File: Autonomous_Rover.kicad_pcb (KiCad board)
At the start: 2 copper layers, 112 x 65 mm, 40 parts, among them M2_1 MountingHole_Pad, M2_2 MountingHole_Pad, M2_3 MountingHole_Pad, Q1 AO3400A, Q2 AO3400A

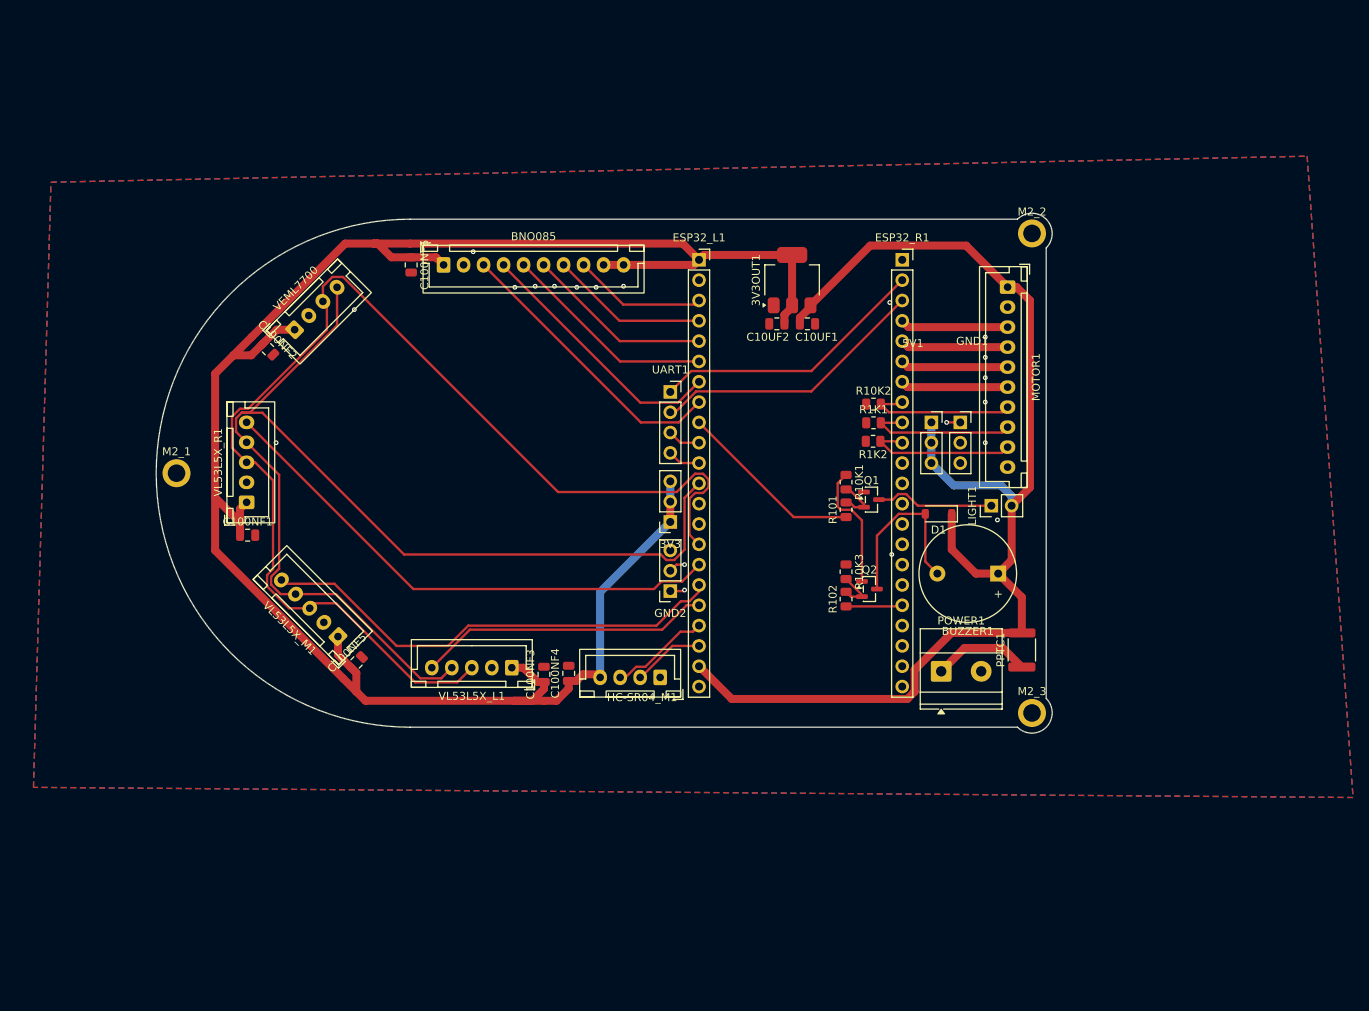
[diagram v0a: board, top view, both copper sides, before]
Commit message: UART 5V and 3V
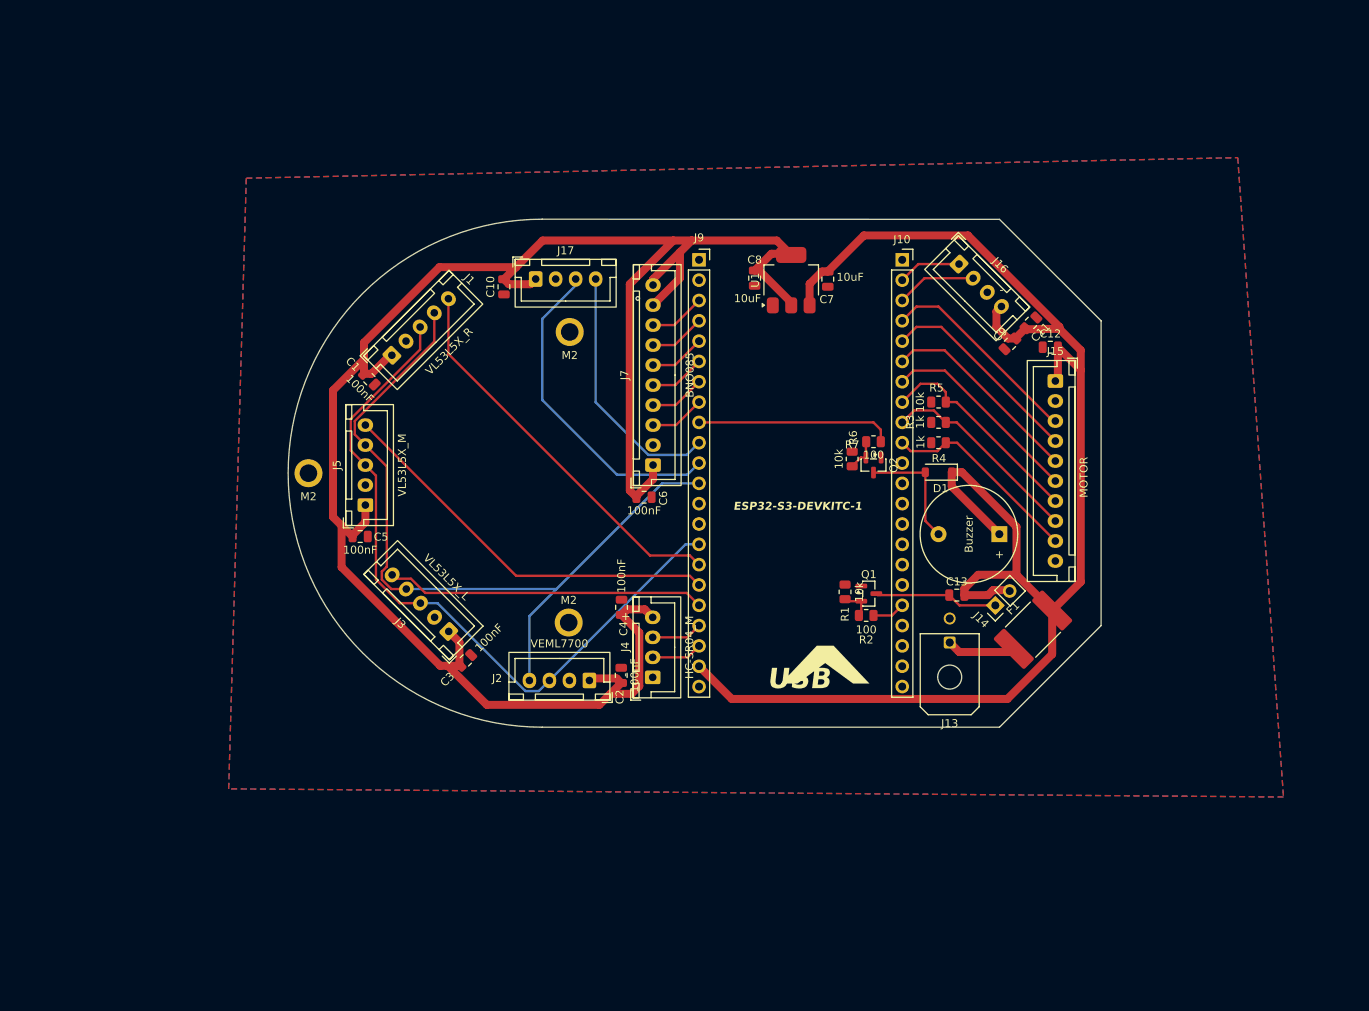
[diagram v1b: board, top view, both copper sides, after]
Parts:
- removed 3V3: 3V Socket, Connector_PinSocket_2.54mm:PinSocket_1x03_P2.54mm_Vertical
- removed 5V1: 5V Socket, Connector_PinSocket_2.54mm:PinSocket_1x03_P2.54mm_Vertical
- removed GND1, GND2: GND, Connector_PinSocket_2.54mm:PinSocket_1x03_P2.54mm_Vertical
- removed PPTC1: Polyfuse, Fuse:Fuse_1812_4532Metric
- removed UART1: EXTRA GPIO, Connector_PinSocket_2.54mm:PinSocket_1x04_P2.54mm_Vertical
- added C10: 100nF, Capacitor_SMD:C_0805_2012Metric, F.Cu at (132.4, 73.2)
- added C11: 10uF, Capacitor_SMD:C_0805_2012Metric, F.Cu at (198.2, 77.7)
- added C12: 100nF, Capacitor_SMD:C_0805_2012Metric, F.Cu at (200.7, 80.8)
- added C13: 10uF, Capacitor_SMD:C_0805_2012Metric, F.Cu at (189.0, 111.8)
- added C9: 100nF, Capacitor_SMD:C_0805_2012Metric, F.Cu at (195.6, 80.4)
- added F1: 2.0A Hold / 3.5A Trip (16V+), Fuse:Fuse_2920_7451Metric, F.Cu at (198.5, 116.1)
- added J16: UART_5V, Connector_JST:JST_XH_B4B-XH-A_1x04_P2.50mm_Vertical, F.Cu at (189.3, 70.4)
- added J17: UART_3V, Connector_JST:JST_XH_B4B-XH-A_1x04_P2.50mm_Vertical, F.Cu at (136.3, 72.2)
- C7: renamed from C10UF1; value 10 micro F -> 10uF
- C8: renamed from C10UF2; value 10 Micro F -> 10uF
- H1: renamed from M2_1; value MountingHole_Pad -> M2
- H2: renamed from M2_2; value MountingHole_Pad -> M2
- H3: renamed from M2_3; value MountingHole_Pad -> M2
- J1: renamed from VL53L5X_R1; value VL53L5X_RIGHT -> VL53L5X_R
- J10: renamed from ESP32_R1; value ESP32_RIGHT -> ESP32_R
- J13: renamed from POWER1; value Power Input -> POWER; footprint TerminalBlock_Phoenix:TerminalBlock_Phoenix_MKDS-1,5-2_1x02_P5.00mm_Horizontal -> Connector_Molex:Molex_Micro-Fit_3.0_43045-0200_2x01_P3.00mm_Horizontal
- J3: renamed from VL53L5X_L1; value VL53L5X_LEFT -> VL53L5X_L
- J4: renamed from HC-SR04_M1; value HC-SR04_MID -> HC-SR04_M
- J5: renamed from VL53L5X_M1; value VL53L5X_MID -> VL53L5X_M
- J9: renamed from ESP32_L1; value ESP32_LEFT -> ESP32_L
- R1: renamed from R10K1; value ~ -> 10k
- moved C2 60.1 mm to (147.0, 121.8), turned to 90 degrees
- moved H2 59.1 mm to (140.6, 78.9)
- moved H3 59.0 mm to (140.5, 115.2)
- moved J2 57.3 mm to (143.0, 122.4), turned to 180 degrees
- moved C6 41.1 mm to (149.9, 99.5), turned to 0 degrees
- moved J7 36.2 mm to (151.0, 95.5), turned to 90 degrees
- moved J1 25.8 mm to (118.4, 81.8), turned to 45 degrees
- moved C1 24.7 mm to (115.5, 84.8), turned to -45 degrees
- moved R7 20.0 mm to (178.6, 92.6), turned to 180 degrees
- moved J5 16.8 mm to (115.0, 100.5), turned to 90 degrees
- moved H1 16.5 mm to (107.9, 96.5)
- moved C5 15.7 mm to (114.4, 104.4), turned to 0 degrees
- moved Q2 15.5 mm to (178.6, 95.5), turned to -90 degrees
- moved R6 14.1 mm to (175.9, 94.7)
- moved R1 13.7 mm to (175.0, 111.4)
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- renumbered BUZZER1 to BZ1, C100NF1 to C1, C100NF2 to C2, C100NF3 to C3, C100NF4 to C4, C100NF5 to C5, C100NF6 to C6, LIGHT1 to J14, MOTOR1 to J15, VEML7700 to J2, BNO085 to J7, R101 to R2, R1K1 to R3, R1K2 to R4, R10K2 to R5, R10K3 to R6, R102 to R7, 3V3OUT1 to U1
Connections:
- H1 pad 1: unconnected-(M2_1-Pad1) -> GND
- H2 pad 1: unconnected-(M2_2-Pad1) -> GND
- H3 pad 1: unconnected-(M2_3-Pad1) -> GND
- J10 pad 18: /BUZZ -> /LIGHT_PWM
- J9 pad 1: +3V3 -> unconnected-(J9-Pin_1-Pad1)
- J9 pad 9: /LIGHT_EN -> /BUZZ_PWM
- R2 pad 1: /LIGHT_EN -> /LIGHT_PWM
- R7 pad 1: /BUZZ -> /BUZZ_PWM
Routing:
- net SCL: track 149.3 -> 90.2 mm
- net SDA: track 146.2 -> 97.8 mm
- net +5V: track 157.2 -> 200.5 mm
- net /UART1_RX: track 4.12 -> 40.9 mm
- net /GPIO8: track 36.2 -> 6.94 mm
- net /UART1_TX: track 4.12 -> 31.7 mm
- net /UART0_TX: track 34.8 -> 7.93 mm
- net /GPIO7: track 32.7 -> 6.96 mm
- net /UART0_RX: track 34.8 -> 10.0 mm
- net /BUZZ_PWM: track 0.00 -> 24.6 mm
- net /LIGHT_EN: track 23.3 -> 0.00 mm
- net GND: track 21.4 -> 0.00 mm, vias 20 -> 1
- net /GPIO6: track 26.9 -> 6.97 mm
- net /LPN_R: track 66.4 -> 49.1 mm
- net /CS: track 23.4 -> 6.99 mm
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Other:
- board size 112 x 65 mm -> 101.6 x 63.5 mm
- board text added: "+"
- board text added: "-"
- board text added: "ESP32-S3-DEVKITC-1"
- board text added: "USB"
- board text added: "^"

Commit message: Design change
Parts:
- moved H3 0.92 mm to (139.7, 114.7)
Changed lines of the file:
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@@
 	(footprint "MountingHole:MountingHole_2.2mm_M2_ISO7380_Pad"
 		(layer "F.Cu")
-		(at 140.462 115.189)
+		(at 139.7 114.681)
 		(descr "Mounting Hole 2.2mm, M2, generated by kicad-footprint-generator mountinghole.py")
 		(tags "mountinghole M2 ISO7380")

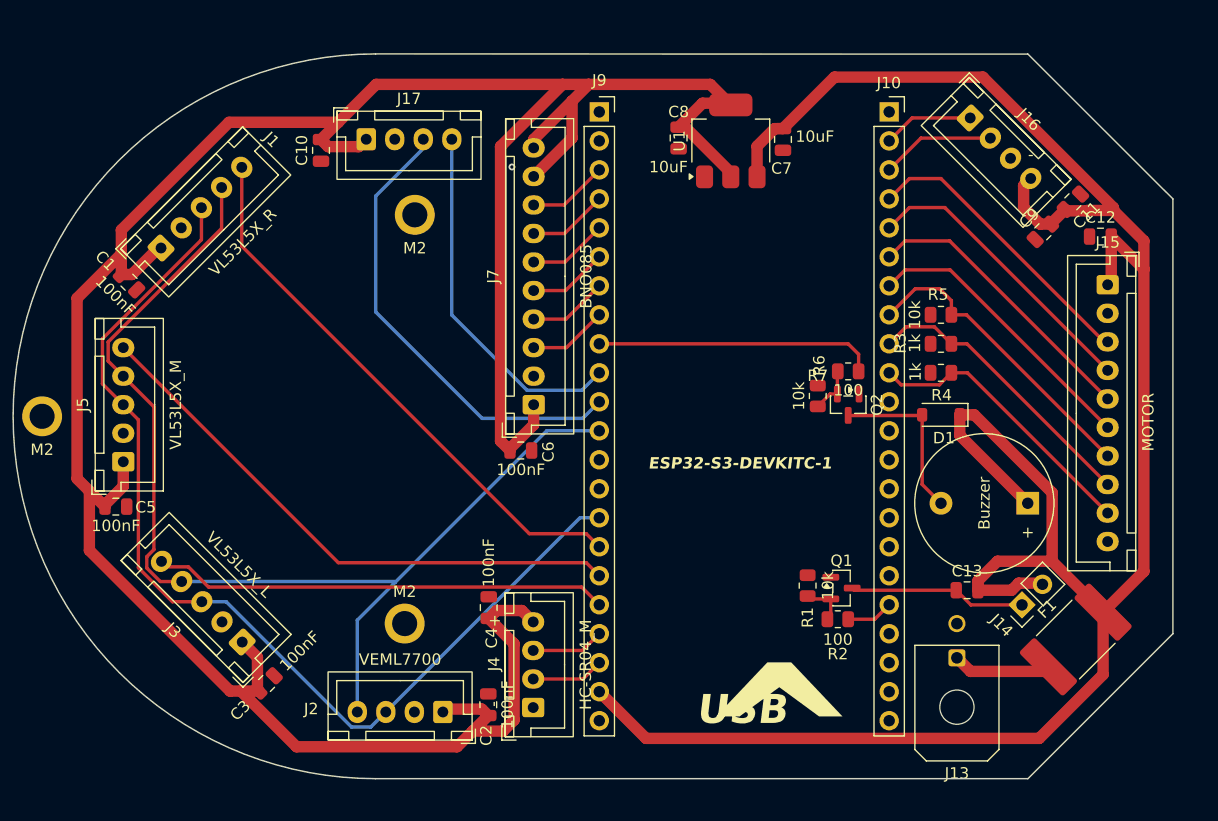
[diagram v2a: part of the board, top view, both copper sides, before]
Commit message: Reorganize Schematic
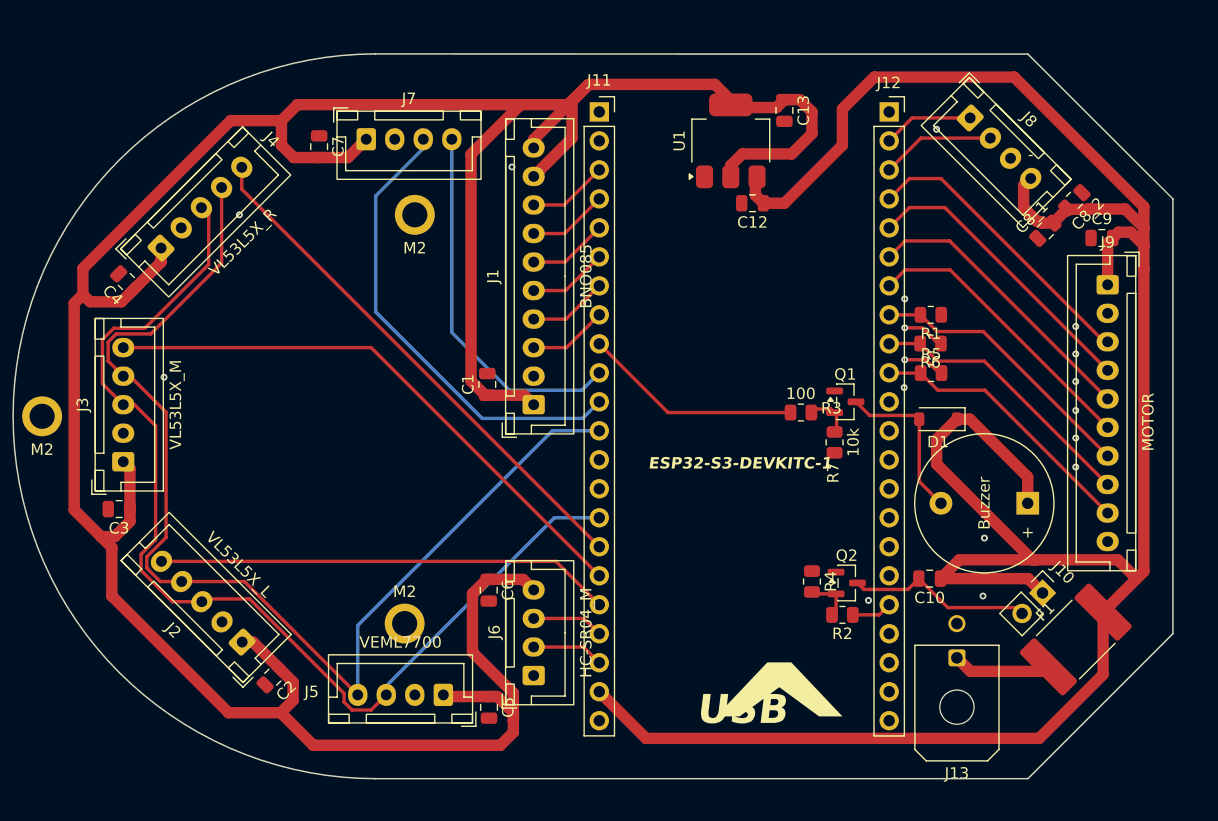
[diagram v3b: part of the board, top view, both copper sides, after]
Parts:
- removed the C10 at (132.4, 73.2)
- removed C11, C8: 10uF, Capacitor_SMD:C_0805_2012Metric
- removed the R3 at (186.7, 90.2)
- added C13: 10uF, Capacitor_SMD:C_0805_2012Metric, F.Cu at (173.0, 69.7)
- added C8_1: 100nF, Capacitor_SMD:C_0805_2012Metric, F.Cu at (195.8, 80.3)
- added C8_2: 10uF, Capacitor_SMD:C_0805_2012Metric, F.Cu at (198.4, 77.6)
- added R6: 1k, Resistor_SMD:R_0805_2012Metric, F.Cu at (185.8, 90.1)
- C12: value 100nF -> 10uF
- C7: value 10uF -> 100nF
- R4: value 1k -> 10k
- R5: value 10k -> 1k
- moved C4 42.7 mm to (115.3, 84.7), turned to 135 degrees
- moved C7 40.6 mm to (132.2, 72.9)
- moved C5 37.1 mm to (147.1, 122.0), turned to -90 degrees
- moved C1 32.6 mm to (146.9, 93.7), turned to 90 degrees
- moved C12 30.6 mm to (170.2, 77.9), turned to 180 degrees
- moved R1 26.1 mm to (185.8, 87.6), turned to 180 degrees
- moved R4 21.5 mm to (175.4, 111.0), turned to -90 degrees
- moved C3 20.0 mm to (114.7, 104.6), turned to 180 degrees
- moved C2 19.0 mm to (128.1, 119.4), turned to -135 degrees
- moved Q1 16.3 mm to (178.3, 95.2)
- moved Q2 15.6 mm to (178.4, 111.1), turned to 0 degrees
- moved C6 12.6 mm to (147.1, 111.8), turned to -90 degrees
- moved R3 5.49 mm to (174.4, 96.2), turned to 0 degrees
- moved C9 5.20 mm to (200.8, 80.9), turned to 0 degrees
- moved R5 5.18 mm to (185.8, 92.7)
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- renumbered C13 to C10, J7 to J1, J14 to J10, J9 to J11, J10 to J12, J3 to J2, J5 to J3, J1 to J4, J2 to J5, J4 to J6, J17 to J7, J16 to J8, J15 to J9, R7 to R3, R6 to R7
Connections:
- C10 pad 1: Net-(J14-Pin_1) -> +5V
- C10 pad 2: +5V -> Net-(J10-Pin_2)
- C12 pad 1: GND -> +5V
- C12 pad 2: +5V -> GND
- C7 pad 1: +5V -> GND
- C7 pad 2: GND -> +3V3
- J10 pad 1: Net-(J14-Pin_1) -> +5V
- J10 pad 2: +5V -> Net-(J10-Pin_2)
- Q1 pad 3: Net-(J14-Pin_1) -> Net-(BZ1--)
- Q2 pad 3: Net-(BZ1--) -> Net-(J10-Pin_2)
- R1 pad 2: Net-(Q1-G) -> /MOT_EN
- R2 pad 2: Net-(Q1-G) -> Net-(Q2-G)
- R3 pad 2: Net-(Q2-G) -> Net-(Q1-G)
- R4 pad 1: /R_IS -> GND
- R4 pad 2: GND -> Net-(Q2-G)
- R5 pad 1: GND -> /R_IS
- R5 pad 2: /MOT_EN -> GND
- R7 pad 2: Net-(Q2-G) -> Net-(Q1-G)
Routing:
- net +3V3: track 248.6 -> 268.4 mm
- net Net-(J10-Pin_2): track 0.00 -> 16.3 mm
- net +5V: track 200.5 -> 216.3 mm
- net Net-(J14-Pin_1): track 15.5 -> 0.00 mm
- net GND: track 0.00 -> 7.45 mm, vias 1 -> 17
- net /BUZZ_PWM: track 24.6 -> 19.2 mm
- net SCL: track 90.2 -> 93.8 mm
- net /LPN_R: track 49.1 -> 46.2 mm
- net /MOT_EN: track 26.9 -> 24.3 mm
- net SDA: track 97.8 -> 99.8 mm
- net /L_IS: track 25.5 -> 24.3 mm
- net /UART1_TX: track 31.7 -> 32.6 mm
- net /R_IS: track 25.1 -> 24.2 mm
- net Net-(BZ1--): track 14.9 -> 14.3 mm
- net /LIGHT_PWM: track 4.12 -> 3.55 mm
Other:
- board text removed: "+"
